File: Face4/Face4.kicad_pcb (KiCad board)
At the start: 2 copper layers, 99.1 x 99.1 mm, 18 parts, among them J1 Conn_01x02, J2 Conn_01x02, J3 Conn_02x04_Counter_Clockwise, J4 Conn_02x04_Counter_Clockwise, SW1 SW_Push, SW2 SW_Push

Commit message: Changed to multiple AS1105 for LED drivers
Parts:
- removed R1, R2: 10k, Resistor_SMD:R_0603_1608Metric
- J1: value Conn_01x02 -> Conn_01x03_Male; footprint Connector_Hirose:Hirose_DF13-02P-1.25DSA_1x02_P1.25mm_Vertical -> Connector_Hirose:Hirose_DF13-03P-1.25DSA_1x03_P1.25mm_Vertical
- J2: value Conn_01x02 -> Conn_02x04_Odd_Even; footprint Connector_Hirose:Hirose_DF13-02P-1.25DSA_1x02_P1.25mm_Vertical -> Connector_IDC:IDC-Header_2x04_P2.54mm_Vertical
- J3: value Conn_02x04_Counter_Clockwise -> Conn_01x04_Male; footprint Connector_IDC:IDC-Header_2x04_P2.54mm_Vertical -> Connector:FanPinHeader_1x04_P2.54mm_Vertical
- J4: value Conn_02x04_Counter_Clockwise -> Conn_01x03_Male; footprint Connector_IDC:IDC-Header_2x04_P2.54mm_Vertical -> Connector_Hirose:Hirose_DF13-03P-1.25DSA_1x03_P1.25mm_Vertical
- moved J3 103.3 mm to (220.5, 113.7), turned to 0 degrees
- moved J1 71.1 mm to (220.7, 121.3)
- moved J2 64.8 mm to (211.7, 116.2), turned to 0 degrees
- moved J4 57.4 mm to (232.9, 113.2)
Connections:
- D1 pad 1: DIG4 -> DIG0
- D1 pad 2: SEGE -> SEGA
- D10 pad 1: DIG5 -> DIG1
- D10 pad 2: SEGF -> SEGDP
- D2 pad 1: DIG4 -> DIG0
- D2 pad 2: SEGF -> SEGB
- D3 pad 1: DIG4 -> DIG1
- D3 pad 2: SEGG -> SEGA
- D4 pad 1: DIG4 -> DIG1
- D4 pad 2: SEGDP -> SEGB
- D5 pad 1: DIG5 -> DIG1
- D5 pad 2: SEGA -> SEGC
- D6 pad 1: DIG5 -> DIG1
- D6 pad 2: SEGB -> SEGD
- D7 pad 1: DIG5 -> DIG1
- D7 pad 2: SEGC -> SEGE
- D8 pad 1: DIG5 -> DIG1
- D8 pad 2: SEGD -> SEGF
- D9 pad 1: DIG5 -> DIG1
- D9 pad 2: SEGE -> SEGG
- J2 pad 1: GPIO0 -> SEGA
- J2 pad 2: GPIO1 -> SEGDP
- J3 pad 1: SEGA -> DIG0
- J3 pad 2: SEGB -> DIG1
- J3 pad 3: SEGC -> DIG2
- J3 pad 4: SEGD -> DIG3
- J4 pad 1: DIG0 -> GND
- J4 pad 2: DIG1 -> 3.3V
- J4 pad 3: DIG2 -> GPIO1
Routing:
- net DIG1: track 0.00 -> 116.4 mm
- net DIG5: track 115.2 -> 0.00 mm
- net SEGDP: track 62.5 -> 0.00 mm
- net SEGA: track 19.0 -> 62.9 mm, vias 0 -> 1
- net SEGC: track 61.4 -> 19.0 mm
- net SEGF: track 99.6 -> 141.0 mm
- net SEGE: track 96.2 -> 61.4 mm, vias 1 -> 0
- net SEGG: track 32.1 -> 66.2 mm
- net SEGB: track 43.1 -> 63.1 mm
- net DIG4: track 103.4 -> 117.4 mm
- net SEGD: track 40.4 -> 43.1 mm
- net GPIO1: track 57.4 -> 58.0 mm

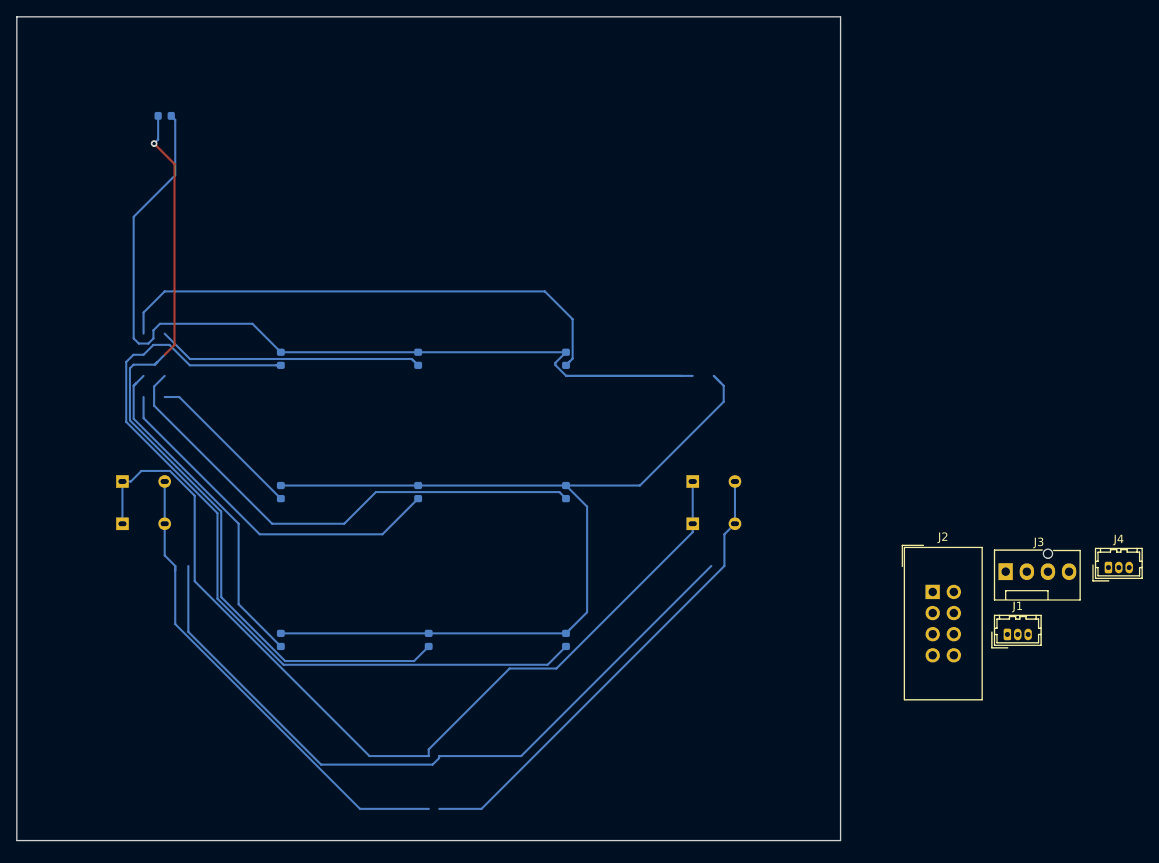
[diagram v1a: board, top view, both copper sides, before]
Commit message: Separated Li-ion charger to face and optimized
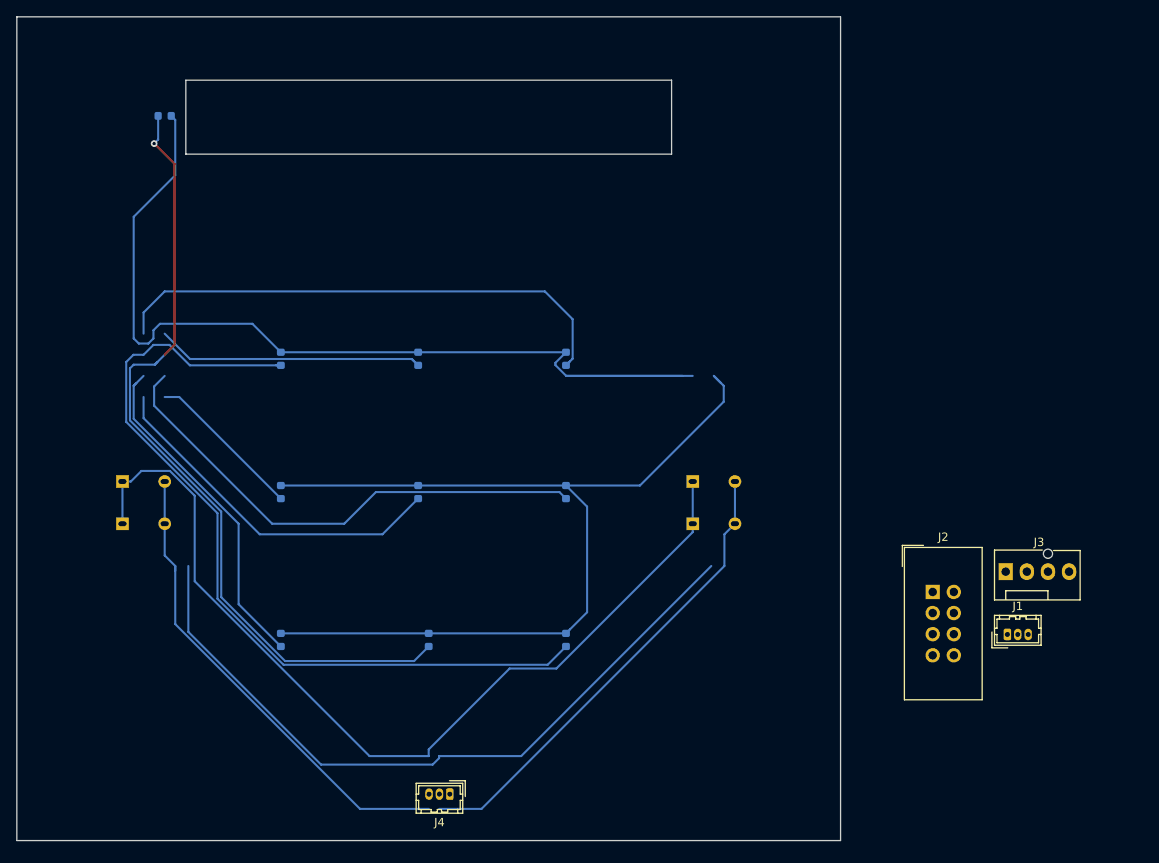
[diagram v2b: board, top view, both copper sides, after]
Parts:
- moved J4 83.8 mm to (153.7, 140.5), turned to 180 degrees
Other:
- outline, holes or cut-outs redrawn
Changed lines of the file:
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@@
   (general
     (thickness 1.6)
-    (drawings 16)
+    (drawings 20)
     (tracks 123)
     (zones 0)
@@
   )
   (module Connector_Hirose:Hirose_DF13-03P-1.25DSA_1x03_P1.25mm_Vertical (layer F.Cu)
-    (at 232.871001 113.215001)
+    (at 153.67 140.462 180)
     (descr "Molex DF13 through hole, DF13-03P-1.25DSA, 3 Pins per row (https://www.hirose.com/product/en/products/DF13/DF13-2P-1.25DSA%2850%29/), generated with kicad-footprint-generator")
     (tags "connector Hirose  side entry")
-    (fp_text reference J4 (at 1.25 -3.4) (layer F.SilkS)
-      (effects (font (size 1 1) (thickness 0.15)))
-    )
-    (fp_text value Conn_01x03_Male (at 1.25 2.4) (layer F.Fab)
-      (effects (font (size 1 1) (thickness 0.15)))
-    )
-    (fp_text user %R (at 1.25 -1.5) (layer F.Fab)
+    (fp_text reference J4 (at 1.25 -3.4 180) (layer F.SilkS)
+      (effects (font (size 1 1) (thickness 0.15)))
+    )
+    (fp_text value Conn_01x03_Male (at 1.25 2.4 180) (layer F.Fab)
+      (effects (font (size 1 1) (thickness 0.15)))
+    )
+    (fp_text user %R (at 1.25 -1.5 180) (layer F.Fab)
       (effects (font (size 1 1) (thickness 0.15)))
     )
@@
     (fp_line (start -1.45 1.2) (end 3.95 1.2) (layer F.Fab) (width 0.1))
     (fp_line (start -1.45 -2.2) (end -1.45 1.2) (layer F.Fab) (width 0.1))
-    (pad 3 thru_hole oval (at 2.5 0) (size 0.9 1.4) (drill 0.6) (layers *.Cu *.Mask)
+    (pad 3 thru_hole oval (at 2.5 0 180) (size 0.9 1.4) (drill 0.6) (layers *.Cu *.Mask)
       (net 12 GPIO1))
-    (pad 2 thru_hole oval (at 1.25 0) (size 0.9 1.4) (drill 0.6) (layers *.Cu *.Mask)
+    (pad 2 thru_hole oval (at 1.25 0 180) (size 0.9 1.4) (drill 0.6) (layers *.Cu *.Mask)
       (net 11 3.3V))
-    (pad 1 thru_hole roundrect (at 0 0) (size 0.9 1.4) (drill 0.6) (layers *.Cu *.Mask) (roundrect_rratio 0.25)
+    (pad 1 thru_hole roundrect (at 0 0 180) (size 0.9 1.4) (drill 0.6) (layers *.Cu *.Mask) (roundrect_rratio 0.25)
       (net 10 GND))
     (model ${KISYS3DMOD}/Connector_Hirose.3dshapes/Hirose_DF13-03P-1.25DSA_1x03_P1.25mm_Vertical.wrl
@@
     )
   )
+  (gr_line (start 121.92 63.5) (end 121.92 54.61) (layer Edge.Cuts) (width 0.05))
+  (gr_line (start 180.34 63.5) (end 121.92 63.5) (layer Edge.Cuts) (width 0.05))
+  (gr_line (start 180.34 54.61) (end 180.34 63.5) (layer Edge.Cuts) (width 0.05))
+  (gr_line (start 121.92 54.61) (end 180.34 54.61) (layer Edge.Cuts) (width 0.05))
   (gr_line (start 180.34 54.61) (end 121.92 54.61) (layer Dwgs.User) (width 0.15))
   (gr_line (start 180.34 63.5) (end 180.34 54.61) (layer Dwgs.User) (width 0.15))
